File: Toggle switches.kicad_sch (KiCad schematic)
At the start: 0 parts

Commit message: 3 pos toggle switch input
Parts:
- added C35, C36: 100nF, 0_capacitors:C_0402_1005Metric, symbol 0_capacitors:CL05B104KO5NNNC
- added R36, R38: 5.1kΩ, 0_resistors:R_0402_1005Metric, symbol 0_resistors:0402WGF5101TCE
- added R37, R39: 47kΩ, 0_resistors:R_0402_1005Metric, symbol 0_resistors:0402WGF4702TCE
- added SW7: SW_SPDT_MSM, 0_connectors:JST_PH_B3B-PH-K_1x03_P2.00mm_Vertical, symbol 0_switches:SW_SPDT_MSM
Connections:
- new net: C35.1, R36.2, R37.2, SW7.3 (4)
- new net: C36.1, R38.2, R39.2, SW7.1
- new net +3.3V: R37.1, R39.1
- new net GND: C35.2, C36.2, SW7.2 (3)
- new net TOGGLE0: R36.1
- new net TOGGLE1: R38.1
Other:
- title: (none) -> UI - Toggle switches

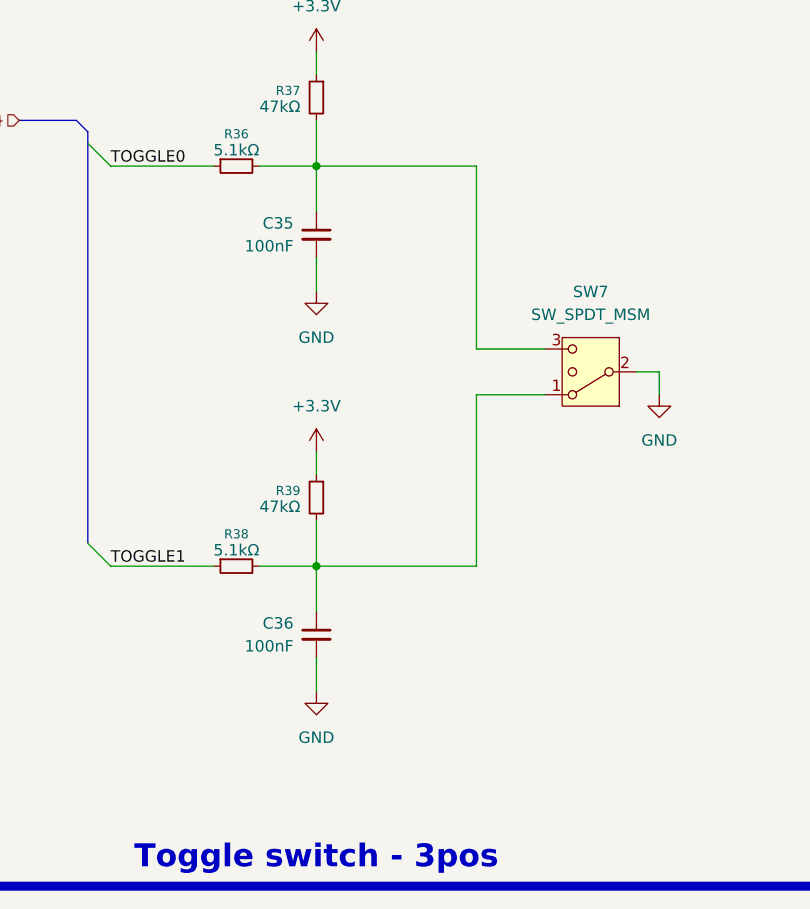
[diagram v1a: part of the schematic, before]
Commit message: added tvs diodes to protect inputs + final component placement
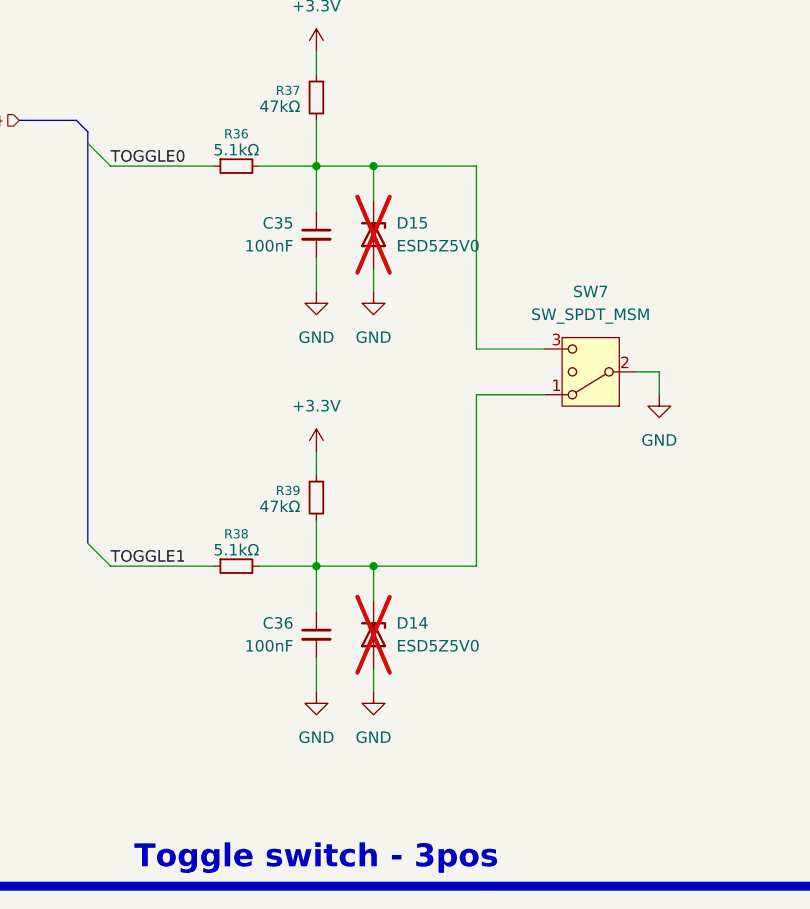
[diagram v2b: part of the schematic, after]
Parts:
- added D14, D15: ESD5Z5V0, 0_diodes:D_SOD-523, symbol 0_diodes:ESD5Z5V0
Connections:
- net GND: now also D14.2 (A), D15.2 (A)
- net at C35.1, R36.2, R37.2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: now also D15.1 (K)
- net at C36.1, R38.2, R39.2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: now also D14.1 (K)

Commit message: designator chagnes and cleanup silkscreen
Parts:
- C35, C36: LCSC PN (none) -> C1525
- D14, D15: LCSC PN (none) -> C191023
- R36, R38: LCSC PN (none) -> C25905
- R37, R39: LCSC PN (none) -> C25792
- SW7: LCSC PN (none) -> C131339
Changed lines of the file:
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@@
+			)
+		)
+		(property "LCSC PN" "C1525"
+			(at 146.05 71.12 0)
+			(effects
+				(font
+					(size 1.27 1.27)
+				)
+				(hide yes)
 			)
 		)
@@
 			)
 		)
+		(property "LCSC PN" "C1525"
+			(at 146.05 115.57 0)
+			(effects
+				(font
+					(size 1.27 1.27)
+				)
+				(hide yes)
+			)
+		)
 		(pin "1"
 		)
@@
 			)
 		)
+		(property "LCSC PN" "C25905"
+			(at 137.16 63.5 0)
+			(effects
+				(font
+					(size 1.27 1.27)
+				)
+				(hide yes)
+			)
+		)
 		(pin "2"
 		)
@@
 		)
 		(property "Supplier Part Number 1" "C25905"
+			(at 137.16 107.95 0)
+			(effects
+				(font
+					(size 1.27 1.27)
+				)
+				(hide yes)
+			)
+		)
+		(property "LCSC PN" "C25905"
 			(at 137.16 107.95 0)
 			(effects
@@
 			)
 		)
+		(property "LCSC PN" "C25792"
+			(at 146.05 55.88 0)
+			(effects
+				(font
+					(size 1.27 1.27)
+				)
+				(hide yes)
+			)
+		)
 		(pin "1"
 		)
@@
 			)
 		)
+		(property "LCSC PN" "C191023"
+			(at 152.4 115.57 0)
+			(effects
+				(font
+					(size 1.27 1.27)
+				)
+				(hide yes)
+			)
+		)
 		(pin "2"
 		)
@@
 			)
 		)
+		(property "LCSC PN" "C25792"
+			(at 146.05 100.33 0)
+			(effects
+				(font
+					(size 1.27 1.27)
+				)
+				(hide yes)
+			)
+		)
 		(pin "1"
 		)
@@
 			)
 		)
+		(property "LCSC PN" "C191023"
+			(at 152.4 71.12 0)
+			(effects
+				(font
+					(size 1.27 1.27)
+				)
+				(hide yes)
+			)
+		)
 		(pin "2"
 		)
@@
 			(at 176.53 86.36 0)
 			(effects
+				(font
+					(size 1.27 1.27)
+				)
+				(hide yes)
+			)
+		)
+		(property "LCSC PN" "C131339"
+			(at 176.53 86.36 0)
+			(effects
